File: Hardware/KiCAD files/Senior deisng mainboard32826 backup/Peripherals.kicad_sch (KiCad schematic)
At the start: 41 parts, among them J3 Conn_01x02, J43 USB, J6 JST_1mm_3_Vertical, J7 JST_1mm_3_Vertical, Q20 BC807, SW1 SPDT_Slide_PTH_11.6x4.0mm, SW2 SPDT_Slide_PTH_11.6x4.0mm, SW3 SPDT_Slide_PTH_11.6x4.0mm, SW4 SPDT_Slide_PTH_11.6x4.0mm, SW7 SPDT_Slide_PTH_11.6x4.0mm, U20 RClamp0504FB, U22 AP22816AKEWT

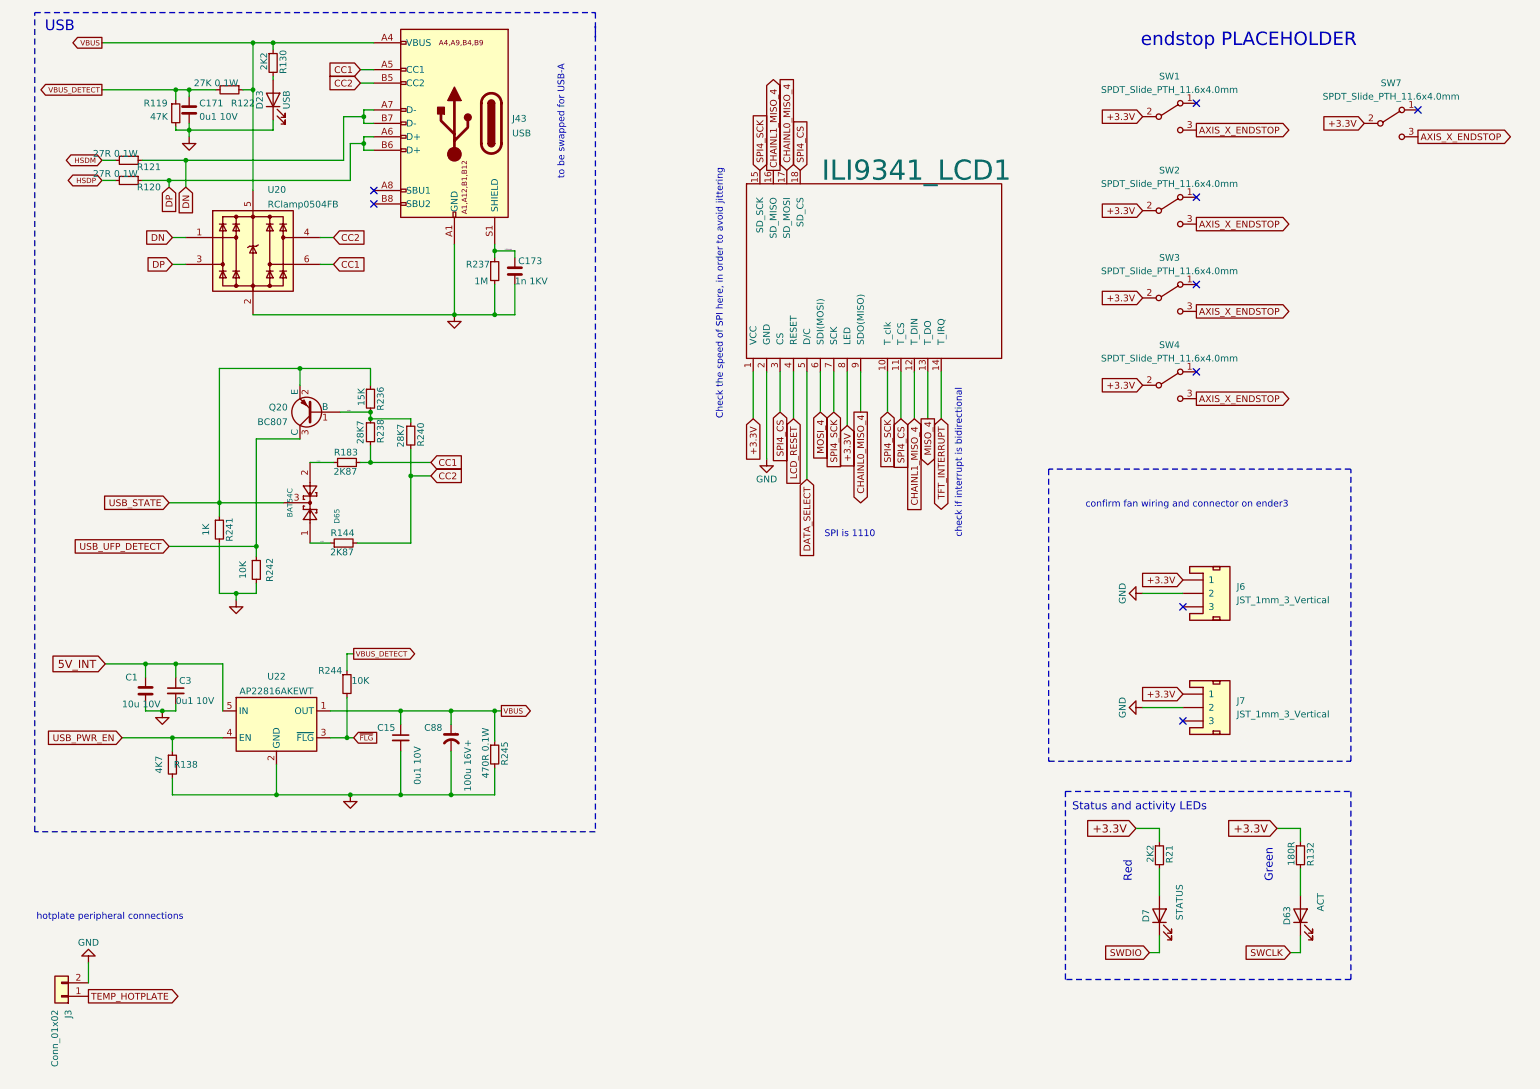
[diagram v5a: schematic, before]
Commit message: swapping connectors and rewiring through the project.
we verified connections with the ender3. a few placeholders replaced.
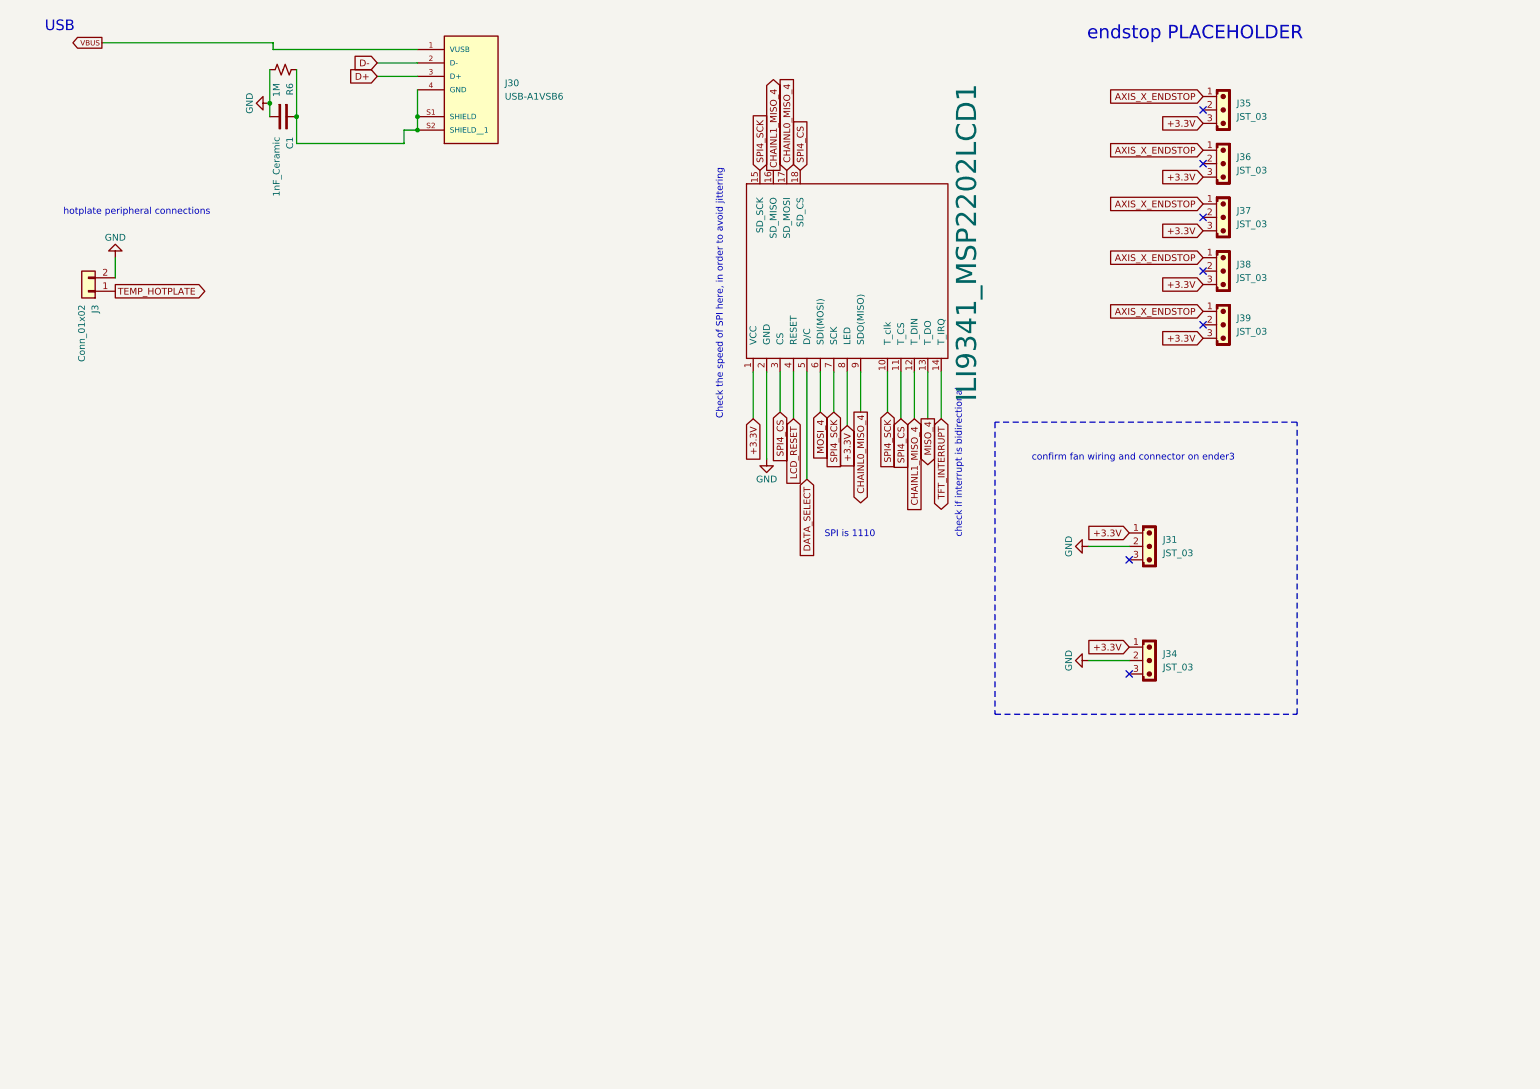
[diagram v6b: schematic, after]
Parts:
- removed C1: 10u 10V, Capacitor_SMD:C_0805_2012Metric, symbol Duet3:C_SMALL
- removed C15, C3: 0u1 10V, Capacitor_SMD:C_0402_1005Metric_Wbry, symbol Device:C_Small
- removed C171: 0u1 10V, Capacitor_SMD:C_0402_1005Metric_Wbry, symbol Duet3:C_SMALL
- removed C173: 1n 1KV, Capacitor_SMD:C_0805_2012Metric, symbol Duet3:C_SMALL
- removed C88: 100u 16V+, Capacitor_SMD:CP_Elec_6.3x7.7, symbol Duet3:C_POL
- removed D23: USB, LED_SMD:LED_0603_1608Metric, symbol Device:LED
- removed D63: ACT, LED_SMD:LED_0603_1608Metric, symbol Device:LED
- removed D65: BAT54C, Package_TO_SOT_SMD:SOT-23, symbol Diode:BAT54C
- removed D7: STATUS, LED_SMD:LED_0603_1608Metric, symbol Device:LED
- removed J43: USB, complib:USB_C_Receptacle_Valcon_CSP-USC16-TR, symbol Duet3:USB_C_Receptacle_USB2.0_16pin
- removed J6, J7: JST_1mm_3_Vertical, PCM_SparkFun-Connector:JST_1x03_P1.0mm_Vertical_SMD, symbol PCM_SparkFun-Connector:Conn_01x03_JST_P1.0mm_Vertical_SMD
- removed Q20: BC807, Package_TO_SOT_SMD:SOT-23, symbol Transistor_BJT:BC807
- removed R119: 47K, Resistor_SMD:R_0402_1005Metric_Wbry, symbol Device:R_Small
- removed R120, R121: 27R 0.1W, Resistor_SMD:R_0402_1005Metric_Wbry, symbol Device:R_Small
- removed R122: 27K 0.1W, Resistor_SMD:R_0402_1005Metric_Wbry, symbol Device:R_Small
- removed R130, R21: 2K2, Resistor_SMD:R_0402_1005Metric_Wbry, symbol Device:R_Small
- removed R132: 180R, Resistor_SMD:R_0402_1005Metric_Wbry, symbol Device:R_Small
- removed R138: 4K7, Resistor_SMD:R_0402_1005Metric_Wbry, symbol Device:R_Small
- removed R144, R183: 2K87, Resistor_SMD:R_0402_1005Metric_Wbry, symbol Device:R_Small
- removed R236: 15K, Resistor_SMD:R_0402_1005Metric_Wbry, symbol Device:R_Small
- removed R237: 1M, Resistor_SMD:R_0805_2012Metric, symbol Device:R_Small
- removed R238, R240: 28K7, Resistor_SMD:R_0402_1005Metric_Wbry, symbol Device:R_Small
- removed R241: 1K, Resistor_SMD:R_0402_1005Metric_Wbry, symbol Device:R_Small
- removed R242, R244: 10K, Resistor_SMD:R_0402_1005Metric_Wbry, symbol Device:R_Small
- removed R245: 470R 0.1W, Resistor_SMD:R_0402_1005Metric_Wbry, symbol Device:R_Small
- removed SW1, SW2, SW3, SW4, SW7: SPDT_Slide_PTH_11.6x4.0mm, PCM_SparkFun-Switch:Slide_SPDT_PTH_11.6x4.0mm, symbol PCM_SparkFun-Switch:SPDT_Slide_PTH_11.6x4.0mm
- removed U20: RClamp0504FB, complib:SC-70-6L, symbol Duet3:RClamp0504FB
- removed U22: AP22816AKEWT, Package_TO_SOT_SMD:SOT-23-5, symbol Power_Management:AP2161W
- added C1: 1nF_Ceramic, Capacitor_THT:C_Disc_D5.0mm_W2.5mm_P2.50mm, symbol PCM_SL_Capacitors:1nF_Ceramic
- added J30: USB-A1VSB6, USB-A1VSB6:ONSHORE_USB-A1VSB6, symbol USB-A1VSB6:USB-A1VSB6
- added J31, J34, J35, J36, J37, J38, J39: JST_03, Connector_JST:JST_EH_B3B-EH-A_1x03_P2.50mm_Vertical, symbol PCM_SL_Connectors:JST_03
- added R6: 1M, PCM_SparkFun-Resistor:R_0603_1608Metric, symbol PCM_SparkFun-Resistor:1M_0603
- renumbered ILI9341_LCD1 to ILI9341_MSP2202LCD1
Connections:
- net +3.3V: now also J31.1, J34.1, J35.3, J36.3, J37.3, J38.3, J39.3
- net AXIS_X_ENDSTOP: now also J35.1, J36.1, J37.1, J38.1, J39.1
- net GND: now also C1.1, J31.2, J34.2, R6.1
- net VBUS: now also J30.1 (VUSB)
- new net: C1.2, J30.4 (GND), J30.S1 (SHIELD), J30.S2 (SHIELD__1), R6.2
- new net D+: J30.3 (D+)
- new net D-: J30.2 (D-)
- no-connect marks 9 -> 7
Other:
- note removed: "Green"
- note removed: "Red"
- note removed: "Status and activity LEDs"
- note removed: "to be swapped for USB-A"
- moved on the sheet: ILI9341_MSP2202LCD1, J3

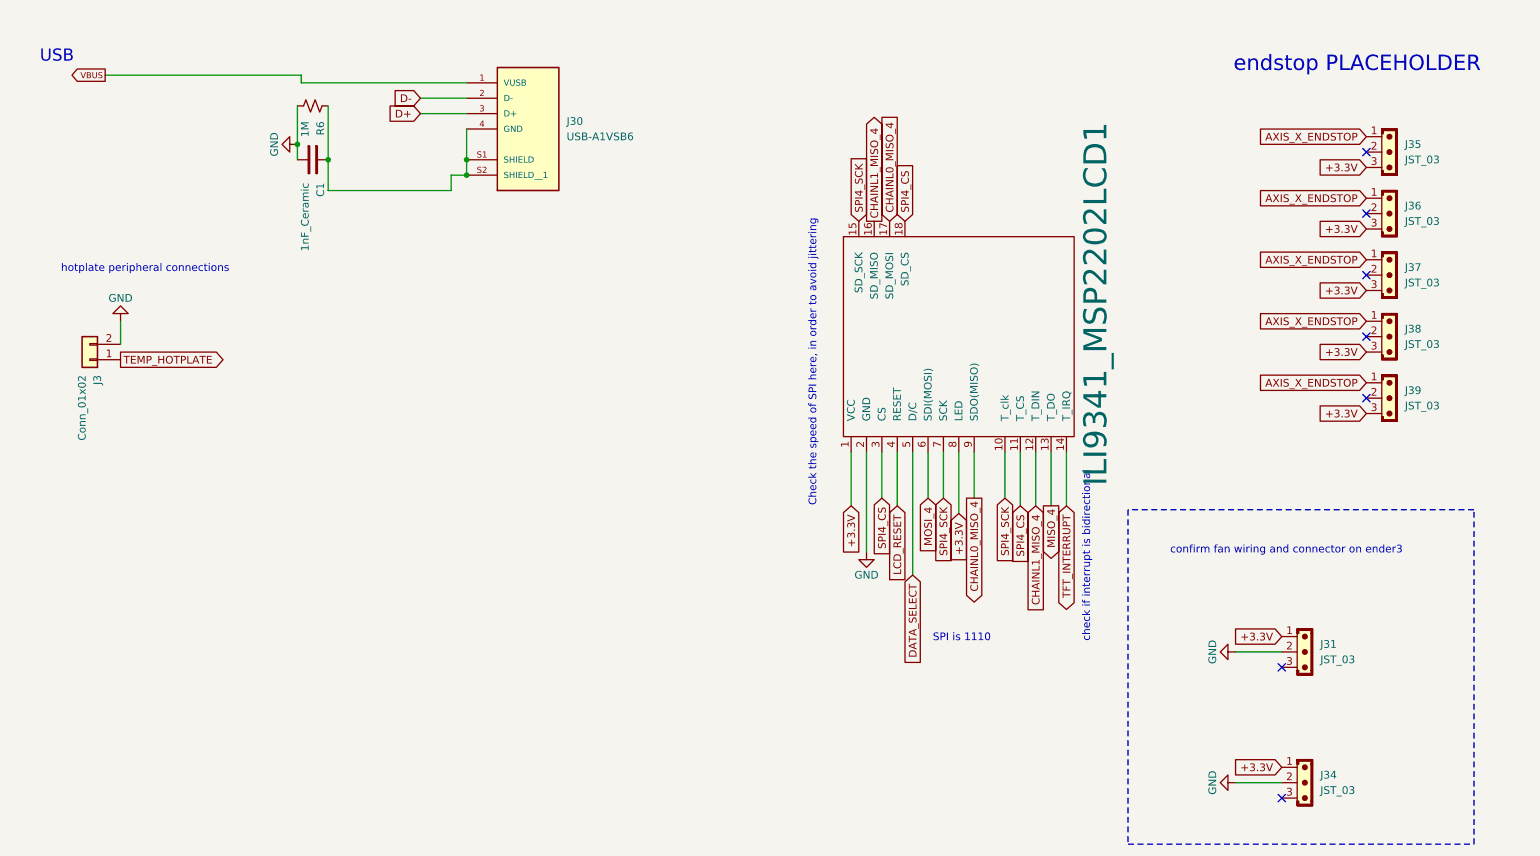
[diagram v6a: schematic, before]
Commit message: New project made to reflect layouts
New project files made in order to generate accurate layouts and create neatness.
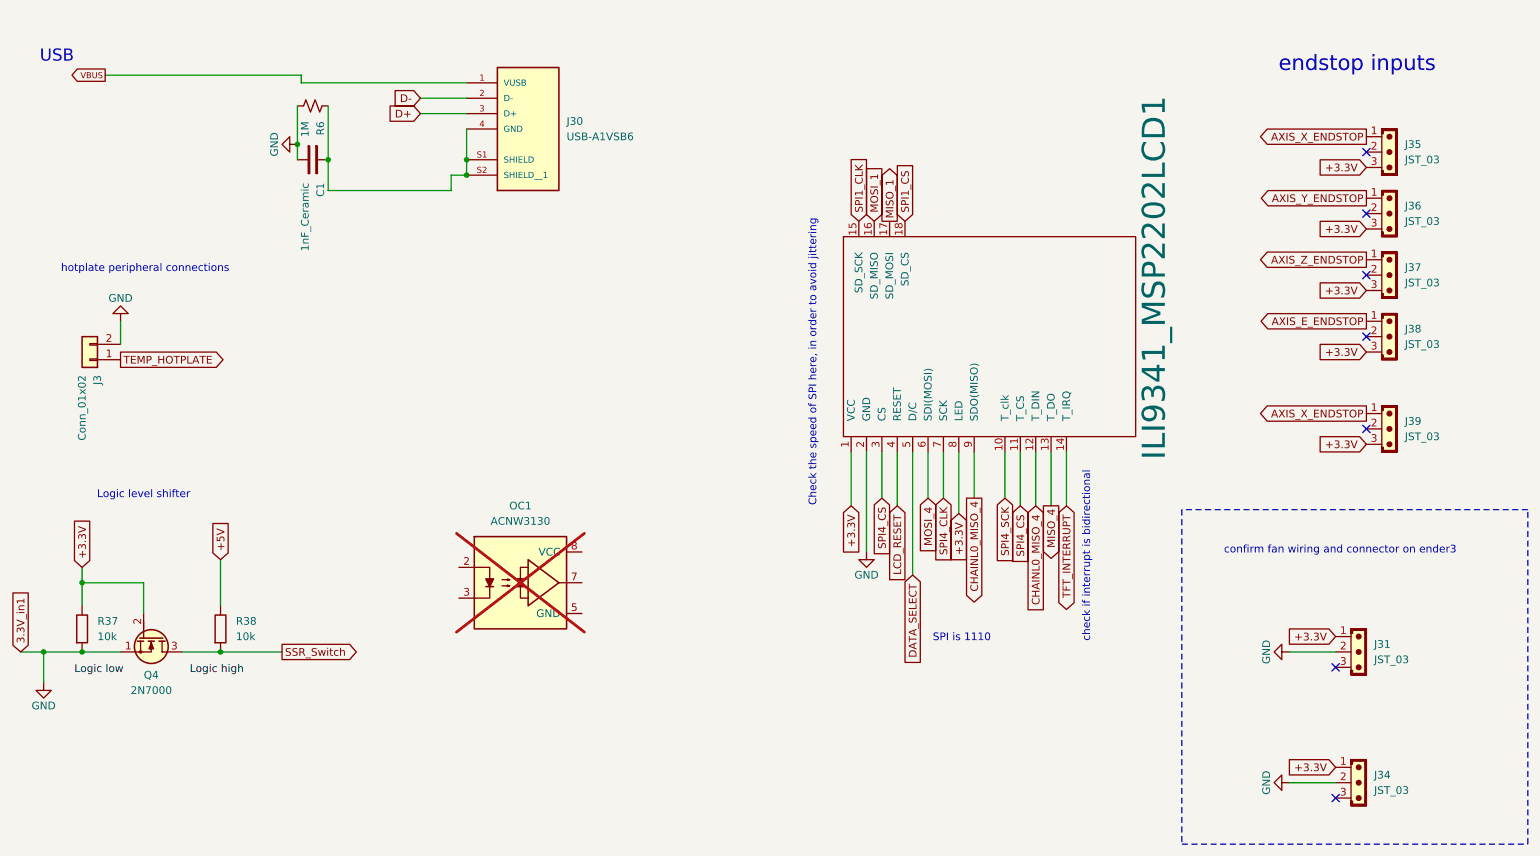
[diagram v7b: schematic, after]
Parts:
- added OC1: ACNW3130, PCM_Package_DIP_AKL:DIP-8_W7.62mm_LongPads, symbol PCM_Optocoupler_Gate_Driver_AKL:ACNW3130
- added Q4: 2N7000, PCM_Package_TO_SOT_THT_AKL:TO-92_Inline_Wide_SGD, symbol PCM_Transistor_MOSFET_AKL:2N7000
- added R37, R38: 10k, Resistor_THT:R_Axial_DIN0207_L6.3mm_D2.5mm_P10.16mm_Horizontal, symbol PCM_SL_Resistors:10k
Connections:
- net +3.3V: now also Q4.2 (G), R37.2
- net AXIS_X_ENDSTOP: no longer J36.1, J37.1, J38.1
- net CHAINL0_MISO_4: now also ILI9341_MSP2202LCD1.12 (T_DIN); no longer ILI9341_MSP2202LCD1.17 (SD_MOSI)
- net GND: now also Q4.1 (S), R37.1
- net SPI4_CS: no longer ILI9341_MSP2202LCD1.18 (SD_CS)
- net SPI4_SCK: no longer ILI9341_MSP2202LCD1.15 (SD_SCK), ILI9341_MSP2202LCD1.7 (SCK)
- net CHAINL1_MISO_4 renamed MOSI_1
- net MOSI_1: no longer ILI9341_MSP2202LCD1.12 (T_DIN)
- new net +5V: R38.2
- new net AXIS_E_ENDSTOP: J38.1
- new net AXIS_Y_ENDSTOP: J36.1
- new net AXIS_Z_ENDSTOP: J37.1
- new net MISO_1: ILI9341_MSP2202LCD1.17 (SD_MOSI)
- new net SPI1_CLK: ILI9341_MSP2202LCD1.15 (SD_SCK)
- new net SPI1_CS: ILI9341_MSP2202LCD1.18 (SD_CS)
- new net SPI4_CLK: ILI9341_MSP2202LCD1.7 (SCK)
- new net SSR_Switch: Q4.3 (D), R38.1
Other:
- note added: "Logic level shifter"
- note added: "endstop inputs"
- note removed: "endstop PLACEHOLDER"
- moved on the sheet: ILI9341_MSP2202LCD1, J31, J34, J39
